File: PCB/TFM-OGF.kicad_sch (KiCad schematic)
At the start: 16 parts, among them J1 Alimentación, J2 CAN, J3 Jumper CAN, J4 Jumper CAN, U1 SN65HVD230, U2 SN65HVD230

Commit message: Finalizo esquemático, usaré medidas y caja de BrakeCAN
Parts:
- removed J2: CAN, symbol Connector_Generic:Conn_01x03
- removed PS1: TSR_2-2450, TSR_2-2450:CONV_TSR_2-2450, symbol TSR_2-2450:TSR_2-2450
- added J10: 5V Output, Connector_JST:JST_XH_B2B-XH-A_1x02_P2.50mm_Vertical, symbol Connector_Generic:Conn_01x02
- added J11: 3.3V Output, Connector_JST:JST_XH_B2B-XH-A_1x02_P2.50mm_Vertical, symbol Connector_Generic:Conn_01x02
- added J2: CAN_Externo, Connector_Dsub:DSUB-9_Socket_Vertical_P2.77x2.84mm_MountingHoles, symbol Connector_Generic:Conn_01x09
- added J5, J7: Lado izquierdo, Connector_PinSocket_2.54mm:PinSocket_1x22_P2.54mm_Vertical, symbol Connector_Generic:Conn_01x22
- added J6, J8: Lado derecho, Connector_PinSocket_2.54mm:PinSocket_1x22_P2.54mm_Vertical, symbol Connector_Generic:Conn_01x22
- added J9: Led_Power_Externo, Connector_JST:JST_XH_B2B-XH-A_1x02_P2.50mm_Vertical, symbol Connector_Generic:Conn_01x02
- added PS1: TSR_1-2450, TSR_1-2450:CONV_TSR_1-2450, symbol TSR_1-2450:TSR_1-2450
- added R11: 200R, Resistor_SMD:R_0603_1608Metric, symbol Device:R
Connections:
- net 3.3V_1: now also J5.21 (Pin_21), J5.22 (Pin_22)
- net 3.3V_2: now also J7.21 (Pin_21), J7.22 (Pin_22)
- net 5V: now also J10.2 (Pin_2), J5.2 (Pin_2), J7.2 (Pin_2), PS1.3 (+VOUT), R11.1
- net CAN_High: now also J2.7 (Pin_7)
- net CAN_Low: now also J2.2 (Pin_2)
- net GND: now also J10.1 (Pin_1), J11.1 (Pin_1), J2.3 (Pin_3), J6.1 (Pin_1), J6.2 (Pin_2), J8.1 (Pin_1), J8.2 (Pin_2), J9.1 (Pin_1), PS1.2 (GND)
- net Vin: now also PS1.1 (+VIN)
- net RxCANDer_G01_2 renamed RxCANDer_G09_2
- net RxCANIzq_G04_1 renamed RxCANIzq_G48_1
- net RxCANIzq_G48_1: now also J6.7 (Pin_7)
- net TxCANDer_G02_2 renamed TxCANDer_G10_2
- net TxCANDer_G10_2: now also J7.7 (Pin_7), J7.8 (Pin_8)
- net TxCANIzq_G05_1 renamed TxCANIzq_G45_1
- net TxCANIzq_G45_1: now also J6.8 (Pin_8)
- new net: J9.2 (Pin_2), R11.2
- new net 3.3V: J11.2 (Pin_2)
- new net G00_1: J6.9 (Pin_9)
- new net G00_2: J8.9 (Pin_9)
- new net G01_1: J6.19 (Pin_19)
- new net G01_2: J8.19 (Pin_19)
- new net G02_1: J6.18 (Pin_18)
- new net G02_2: J8.18 (Pin_18)
- new net G03_1: J5.10 (Pin_10)
- new net G03_2: J7.10 (Pin_10)
- new net G04_1: J5.19 (Pin_19)
- new net G04_2: J7.19 (Pin_19)
- new net G05_1: J5.18 (Pin_18)
- new net G05_2: J7.18 (Pin_18)
- new net G06_1: J5.17 (Pin_17)
- new net G06_2: J7.17 (Pin_17)
- new net G07_1: J5.16 (Pin_16)
- new net G07_2: J7.16 (Pin_16)
- new net G08_1: J5.11 (Pin_11)
- new net G08_2: J7.11 (Pin_11)
- new net G09_1: J5.8 (Pin_8)
- new net G10_1: J5.7 (Pin_7)
- new net G11_1: J5.6 (Pin_6)
- new net G11_2: J7.6 (Pin_6)
- new net G12_1: J5.5 (Pin_5)
- new net G12_2: J7.5 (Pin_5)
- new net G13_1: J5.4 (Pin_4)
- new net G13_2: J7.4 (Pin_4)
- new net G14_1: J5.3 (Pin_3)
- new net G14_2: J7.3 (Pin_3)
- new net G15_1: J5.15 (Pin_15)
- new net G15_2: J7.15 (Pin_15)
- new net G16_1: J5.14 (Pin_14)
- new net G16_2: J7.14 (Pin_14)
- new net G17_1: J5.13 (Pin_13)
- new net G17_2: J7.13 (Pin_13)
- new net G18_1: J5.12 (Pin_12)
- new net G18_2: J7.12 (Pin_12)
- new net G19_1: J6.3 (Pin_3)
- new net G19_2: J8.3 (Pin_3)
- new net G20_1: J6.4 (Pin_4)
- new net G20_2: J8.4 (Pin_4)
- new net G21_1: J6.5 (Pin_5)
- new net G21_2: J8.5 (Pin_5)
- new net G35_1: J6.10 (Pin_10)
- new net G35_2: J8.10 (Pin_10)
- new net G36_1: J6.11 (Pin_11)
- new net G36_2: J8.11 (Pin_11)
- new net G37_1: J6.12 (Pin_12)
- new net G37_2: J8.12 (Pin_12)
- new net G38_1: J6.13 (Pin_13)
- new net G38_2: J8.13 (Pin_13)
- new net G39_1: J6.14 (Pin_14)
- new net G39_2: J8.14 (Pin_14)
- new net G40_1: J6.15 (Pin_15)
- new net G40_2: J8.15 (Pin_15)
- new net G41_1: J6.16 (Pin_16)
- new net G41_2: J8.16 (Pin_16)
- new net G42_1: J6.17 (Pin_17)
- new net G42_2: J8.17 (Pin_17)
- new net G45_2: J8.8 (Pin_8)
- new net G46_1: J5.9 (Pin_9)
- new net G46_2: J7.9 (Pin_9)
- new net G47_1: J6.6 (Pin_6)
- new net G47_2: J8.6 (Pin_6)
- new net G48_2: J8.7 (Pin_7)
- new net GND_1: J5.1 (Pin_1)
- new net GND_2: J6.22 (Pin_22)
- new net GND_3: J7.1 (Pin_1)
- new net GND_4: J8.22 (Pin_22)
- new net RST_1: J5.20 (Pin_20)
- new net RST_2: J7.20 (Pin_20)
- new net RX_1: J6.20 (Pin_20)
- new net RX_2: J8.20 (Pin_20)
- new net TX_1: J6.21 (Pin_21)
- new net TX_2: J8.21 (Pin_21)
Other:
- note added: "CAN 1 (izquierda)"
- note added: "CAN 2 (derecha)"
- note added: "Conectores auxiliares"
- note added: "ESP32-S3 derecho (USBs hacia abajo)"
- note added: "ESP32-S3 izquierdo (USBs hacia abajo)"
- note added: "TFM-OGF"
- note removed: "CAN 1(izquierda)"
- note removed: "CAN 2(derecha)"
- note removed: "Usaré los pines 1, 2, 4 y 5"
- company: (none) -> UNIR
- title: (none) -> TFM-OGF

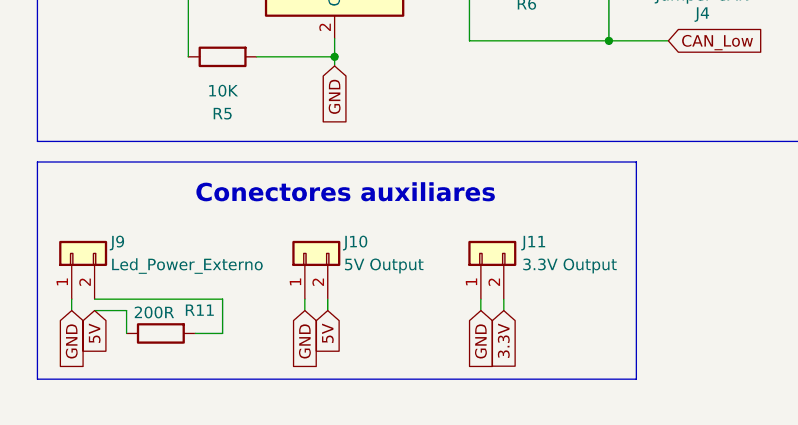
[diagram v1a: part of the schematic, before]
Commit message: Primera versión de colocar los componentes
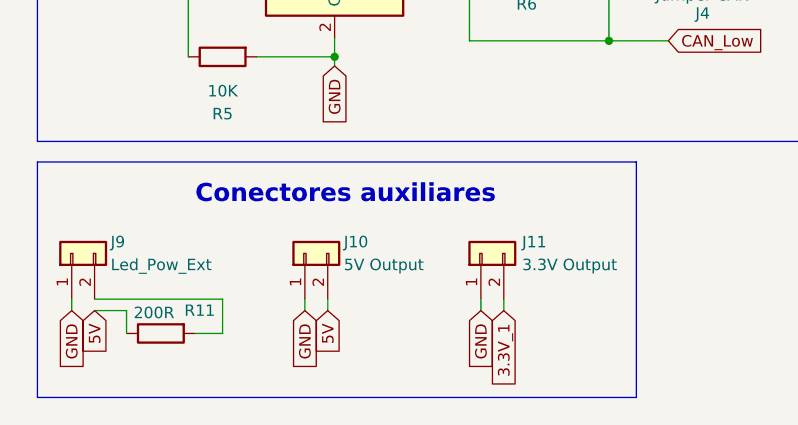
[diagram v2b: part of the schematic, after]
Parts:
- J9: value Led_Power_Externo -> Led_Pow_Ext
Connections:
- net 3.3V is gone; now on net 3.3V_1: J11.2 (Pin_2)
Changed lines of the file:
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@@
 	(rectangle
 		(start 16.256 138.43)
-		(end 82.804 162.56)
+		(end 82.804 164.592)
 		(stroke
 			(width 0)
@@
 		)
 	)
-	(global_label "3.3V"
+	(global_label "3.3V_1"
 		(shape input)
 		(at 68.072 154.94 270)
@@
 		)
 		(property "Intersheetrefs" "${INTERSHEET_REFS}"
-			(at 68.072 161.4328 90)
+			(at 68.072 164.2147 90)
 			(effects
 				(font
@@
 			)
 		)
-		(property "Value" "Led_Power_Externo"
+		(property "Value" "Led_Pow_Ext"
 			(at 24.384 149.86 90)
 			(effects

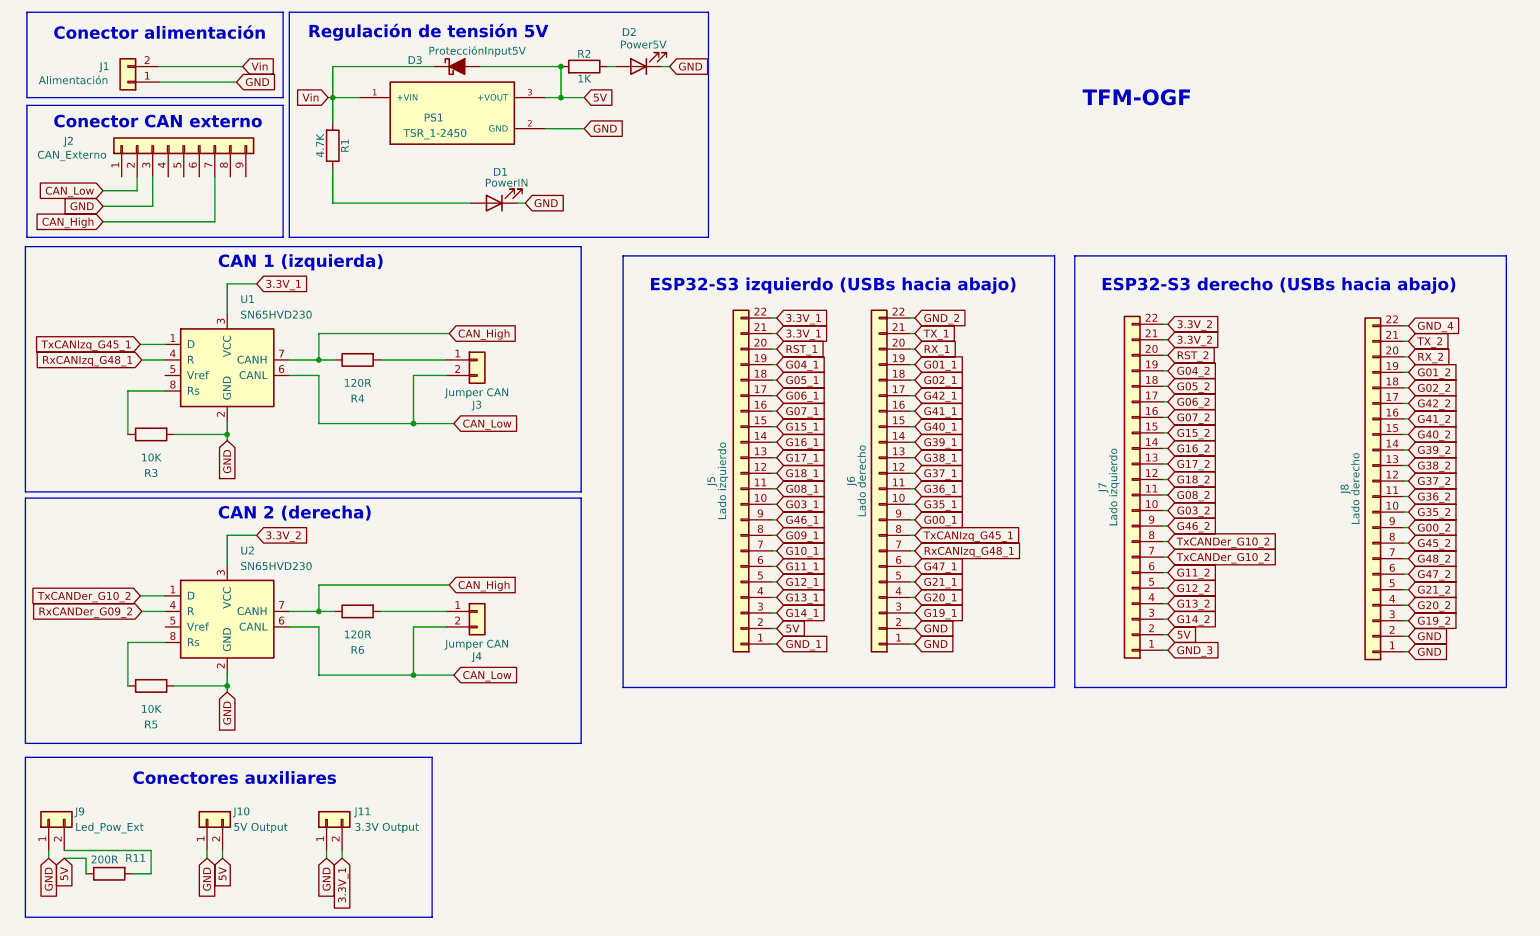
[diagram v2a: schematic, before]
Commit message: Corrijo orientación de algunas resistencias
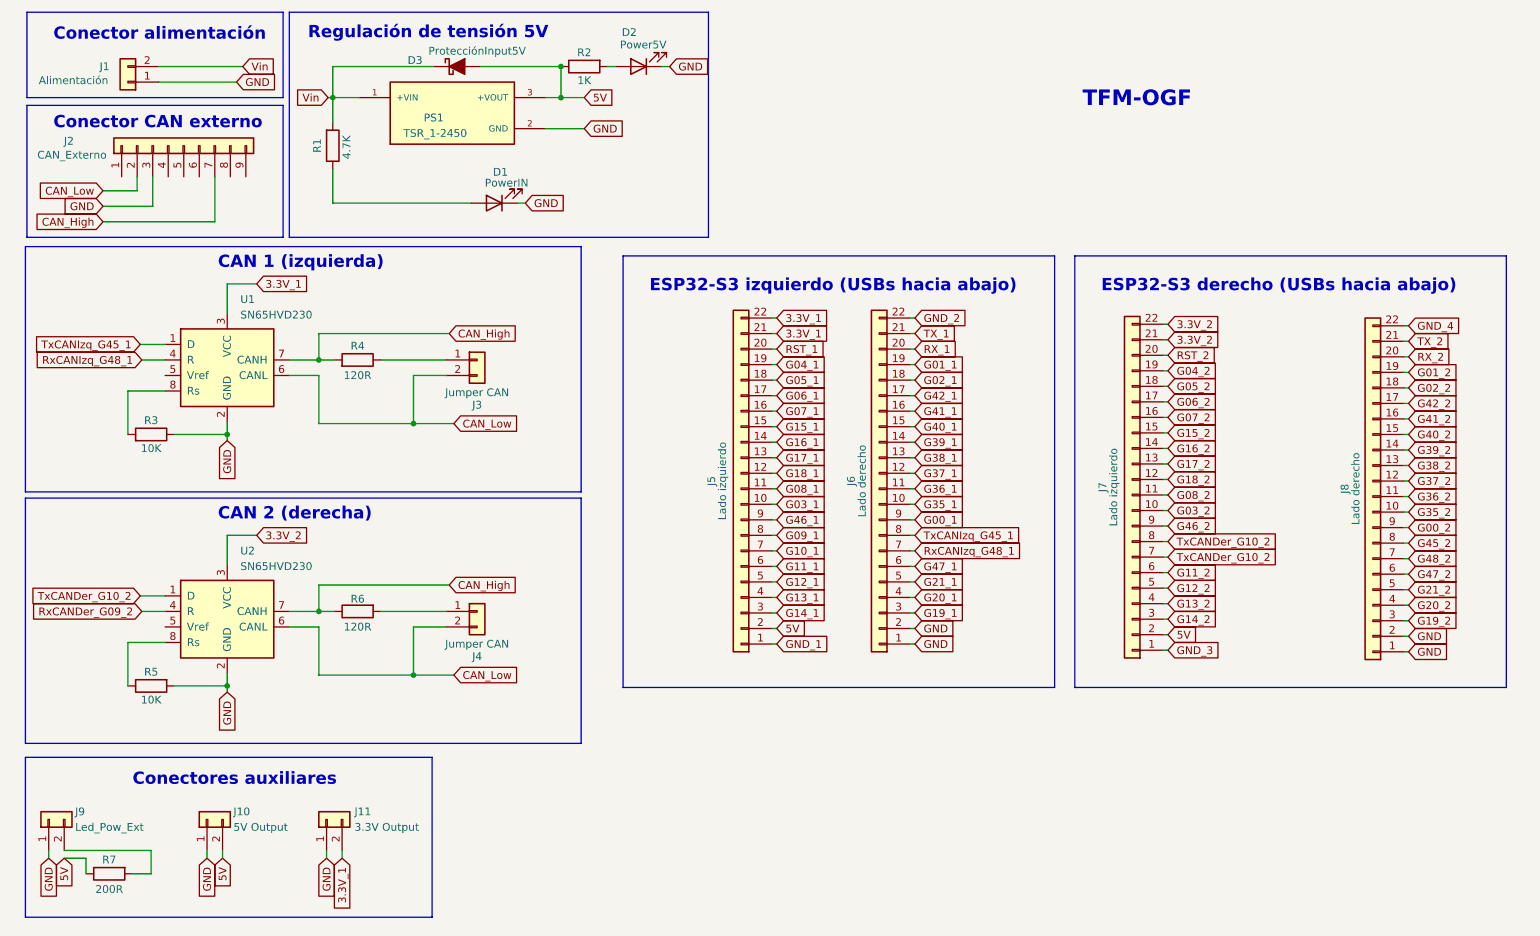
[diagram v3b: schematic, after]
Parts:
- renumbered R11 to R7
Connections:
- net 5V: now also R2.1; no longer R2.2
- net CAN_High: now also R4.2; no longer R4.1
- net GND: now also R3.1; no longer R3.2
- net at D2.2 (A): now also R2.2; no longer R2.1
- net at U1.8 (Rs): now also R3.2; no longer R3.1
- net at J3.1 (Pin_1): now also R4.1; no longer R4.2
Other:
- moved on the sheet: R2, R3, R4
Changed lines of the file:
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@@
 	)
 	(junction
-		(at 66.548 30.48)
+		(at 103.886 25.4)
 		(diameter 0)
 		(color 0 0 0 0)
 	)
 	(junction
-		(at 64.262 114.554)
+		(at 66.548 30.48)
 		(diameter 0)
 		(color 0 0 0 0)
 	)
 	(junction
-		(at 64.262 73.406)
+		(at 64.262 114.554)
 		(diameter 0)
 		(color 0 0 0 0)
 	)
 	(junction
-		(at 103.886 25.4)
+		(at 64.262 73.406)
 		(diameter 0)
 		(color 0 0 0 0)
@@
 		(dnp no)
 		(property "Reference" "R5"
-			(at 36.83 133.096 90)
+			(at 36.83 124.46 90)
 			(effects
 				(font
@@
 		)
 		(property "Value" "10K"
-			(at 36.83 130.556 90)
+			(at 36.83 129.032 90)
 			(effects
 				(font
@@
 	(symbol
 		(lib_id "Device:R")
-		(at 107.696 25.4 270)
+		(at 107.696 25.4 90)
 		(mirror x)
 		(unit 1)
@@
 		(dnp no)
 		(property "Reference" "R2"
-			(at 107.696 23.368 90)
+			(at 107.696 23.114 90)
 			(effects
 				(font
@@
 		)
 		(property "Value" "1K"
-			(at 107.696 27.432 90)
+			(at 107.696 27.686 90)
 			(effects
 				(font
@@
 		)
 		(property "Footprint" "Resistor_SMD:R_0603_1608Metric"
-			(at 107.696 27.178 90)
+			(at 107.696 23.622 90)
 			(effects
 				(font
@@
 		(dnp no)
 		(property "Reference" "R6"
-			(at 70.612 120.904 90)
+			(at 70.612 112.522 90)
 			(effects
 				(font
@@
 		)
 		(property "Value" "120R"
-			(at 70.612 118.364 90)
+			(at 70.612 117.094 90)
 			(effects
 				(font
@@
 		(dnp no)
 		(property "Reference" "R1"
-			(at 68.58 38.354 90)
+			(at 64.008 38.354 90)
 			(effects
 				(font
@@
 		)
 		(property "Value" "4.7K"
-			(at 64.516 38.354 90)
+			(at 68.834 38.608 90)
 			(effects
 				(font
@@
 	(symbol
 		(lib_id "Device:R")
-		(at 70.612 73.406 90)
+		(at 70.612 73.406 270)
 		(mirror x)
 		(unit 1)
@@
 		(dnp no)
 		(property "Reference" "R4"
-			(at 70.612 79.756 90)
+			(at 70.612 71.12 90)
 			(effects
 				(font
@@
 		)
 		(property "Value" "120R"
-			(at 70.612 77.216 90)
+			(at 70.612 75.946 90)
 			(effects
 				(font
@@
 		)
 		(property "Footprint" "Resistor_SMD:R_0603_1608Metric"
-			(at 70.612 71.628 90)
+			(at 70.612 75.184 90)
 			(effects
 				(font
@@
 	(symbol
 		(lib_id "Device:R")
-		(at 36.83 85.598 90)
+		(at 36.83 85.598 270)
 		(mirror x)
 		(unit 1)
@@
 		(dnp no)
 		(property "Reference" "R3"
-			(at 36.83 91.948 90)
+			(at 36.83 83.312 90)
 			(effects
 				(font
@@
 		)
 		(property "Value" "10K"
-			(at 36.83 89.408 90)
+			(at 36.83 87.884 90)
 			(effects
 				(font
@@
 		)
 		(property "Footprint" "Resistor_SMD:R_0603_1608Metric"
-			(at 36.83 83.82 90)
+			(at 36.83 87.376 90)
 			(effects
 				(font
@@
 		(on_board yes)
 		(dnp no)
-		(property "Reference" "R11"
-			(at 34.29 154.94 90)
+		(property "Reference" "R7"
+			(at 29.972 155.194 90)
 			(effects
 				(font
@@
 		)
 		(property "Value" "200R"
-			(at 29.21 155.194 90)
+			(at 29.972 160.02 90)
 			(effects
 				(font
@@
 			(project "TFM-OGF"
 				(path "/41b37644-2050-448d-bbd4-fcd0da7fc3d1"
-					(reference "R11")
+					(reference "R7")
 					(unit 1)
 				)

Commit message: Completo placa
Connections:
- net RxCANDer_G09_2: now also J7.8 (Pin_8)
- net TxCANDer_G10_2: no longer J7.8 (Pin_8)
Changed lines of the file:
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@@
 		)
 	)
-	(global_label "TxCANDer_G10_2"
+	(global_label "RxCANDer_G09_2"
 		(shape input)
 		(at 203.2 103.124 0)
@@
 		)
 		(property "Intersheetrefs" "${INTERSHEET_REFS}"
-			(at 221.8485 103.124 0)
+			(at 222.1509 103.124 0)
 			(effects
 				(font

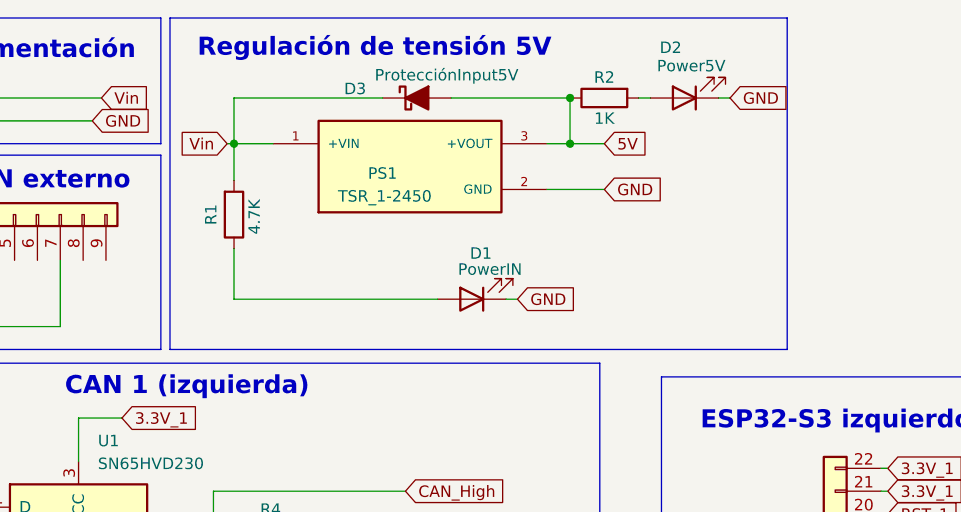
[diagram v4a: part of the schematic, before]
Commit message: Cambio símbolo y huella TSR1 para usar los de KiCad, regenero ficheros de producción
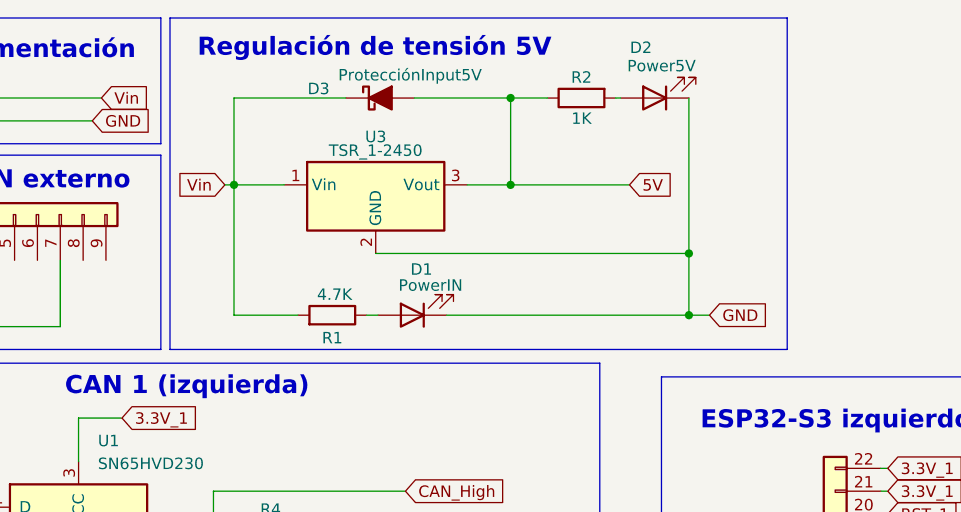
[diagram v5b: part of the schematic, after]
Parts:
- removed PS1: TSR_1-2450, TSR_1-2450:CONV_TSR_1-2450, symbol TSR_1-2450:TSR_1-2450
- added U3: TSR_1-2450, Converter_DCDC:Converter_DCDC_TRACO_TSR-1_THT, symbol Regulator_Switching:TSR_1-2450
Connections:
- net 5V: now also U3.3 (Vout)
- net GND: now also U3.2 (GND)
- net Vin: now also U3.1 (Vin)
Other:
- moved on the sheet: D1, D2, D3, R1, R2
